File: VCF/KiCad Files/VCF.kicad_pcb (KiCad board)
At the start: 2 copper layers, 156.1 x 128.5 mm, 79 parts, among them J1 CV1, J2 CV2, J3 AUDIO_IN, J4 AUDIO_OUT, J5 Conn_02x05_Odd_Even, J6 Conn_01x05_Male, J7 Conn_01x05_Female, J8 Conn_01x08_Male, J9 Conn_01x08_Female, SW1 SW_DPDT_x2, U1 TL074, U2 TL074

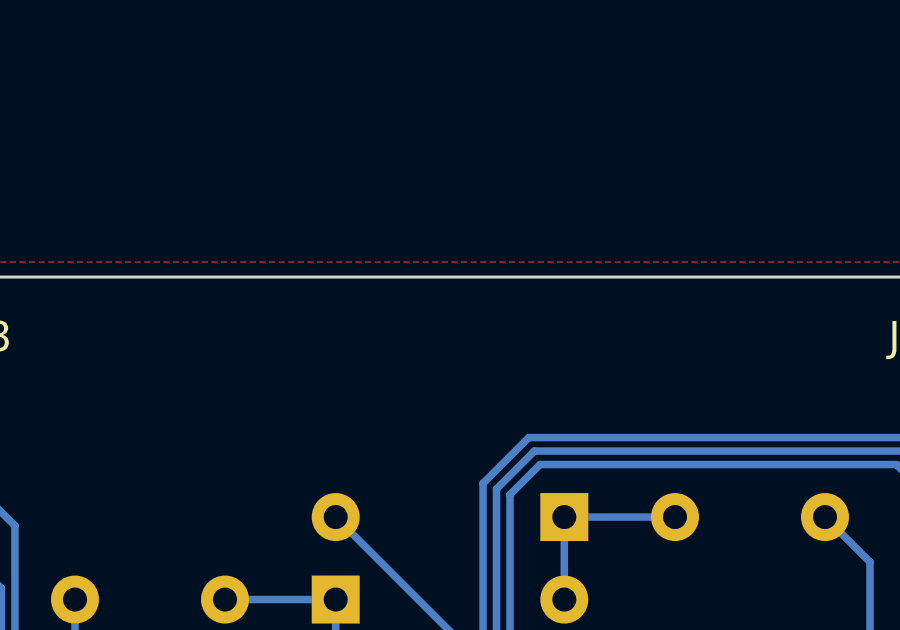
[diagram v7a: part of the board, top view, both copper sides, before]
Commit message: Updated silkscreens
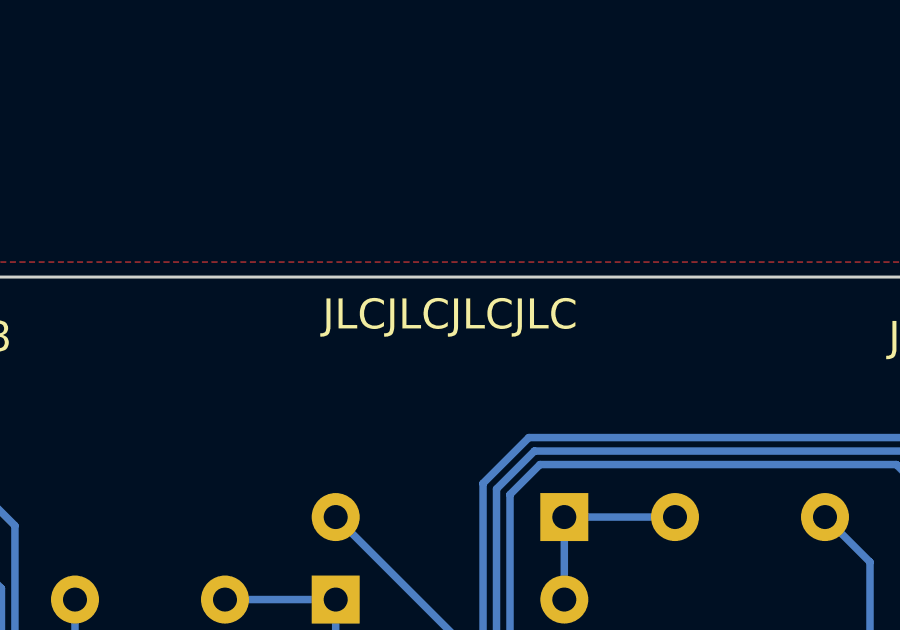
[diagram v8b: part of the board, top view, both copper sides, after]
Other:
- board text added: "JLCJLCJLCJLC"
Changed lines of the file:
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@@
   (gr_rect (start 100 40) (end 140.25 150) (layer "Edge.Cuts") (width 0.1) (fill none))
   (gr_rect (start 43.375 30.75) (end 83.625 159.25) (layer "Edge.Cuts") (width 0.1) (fill none))
+  (gr_text "JLCJLCJLCJLC" (at 120.125 149) (layer "B.SilkS")
+    (effects (font (size 1 1) (thickness 0.15)) (justify mirror))
+  )
+  (gr_text "JLCJLCJLCJLC" (at 63.625 158) (layer "B.SilkS")
+    (effects (font (size 1 1) (thickness 0.15)) (justify mirror))
+  )
   (gr_text "-12V" (at 170.875 135.5 270) (layer "B.SilkS")
     (effects (font (size 1 1) (thickness 0.15)) (justify mirror))
@@
     (effects (font (size 1.5 1.5) (thickness 0.25)))
   )
+  (gr_text "JLCJLCJLCJLC" (at 179.375 48.5) (layer "F.SilkS")
+    (effects (font (size 1 1) (thickness 0.15)))
+  )
   (gr_text "IN" (at 53.375 149) (layer "F.SilkS")
